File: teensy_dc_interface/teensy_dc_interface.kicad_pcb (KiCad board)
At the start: 2 copper layers, 80 x 128.5 mm, 165 parts, among them J1 Chan 1 Out, J10 3.5mm_Mono_Switched_SymSmall_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, J11 Conn_01x03, J12 Conn_01x03, J13 Conn_01x03, J2 Chan 2 Out, J3 Chan 3 Out, J4 Chan 4 Out, J5 Chan 5 Out, J6 Chan 6 Out, J7 Chan 7 Out, J8 Chan 8 Out, J9 3.5mm_Mono_Switched_SymSmall_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, U1 AK4458VN, U2 Teensy4.0, U3 AP65211A, U4 AP62200TWU-7, U5 NE5532, U6 NE5532, U7 NE5532, U8 NE5532, U9 AP65211A

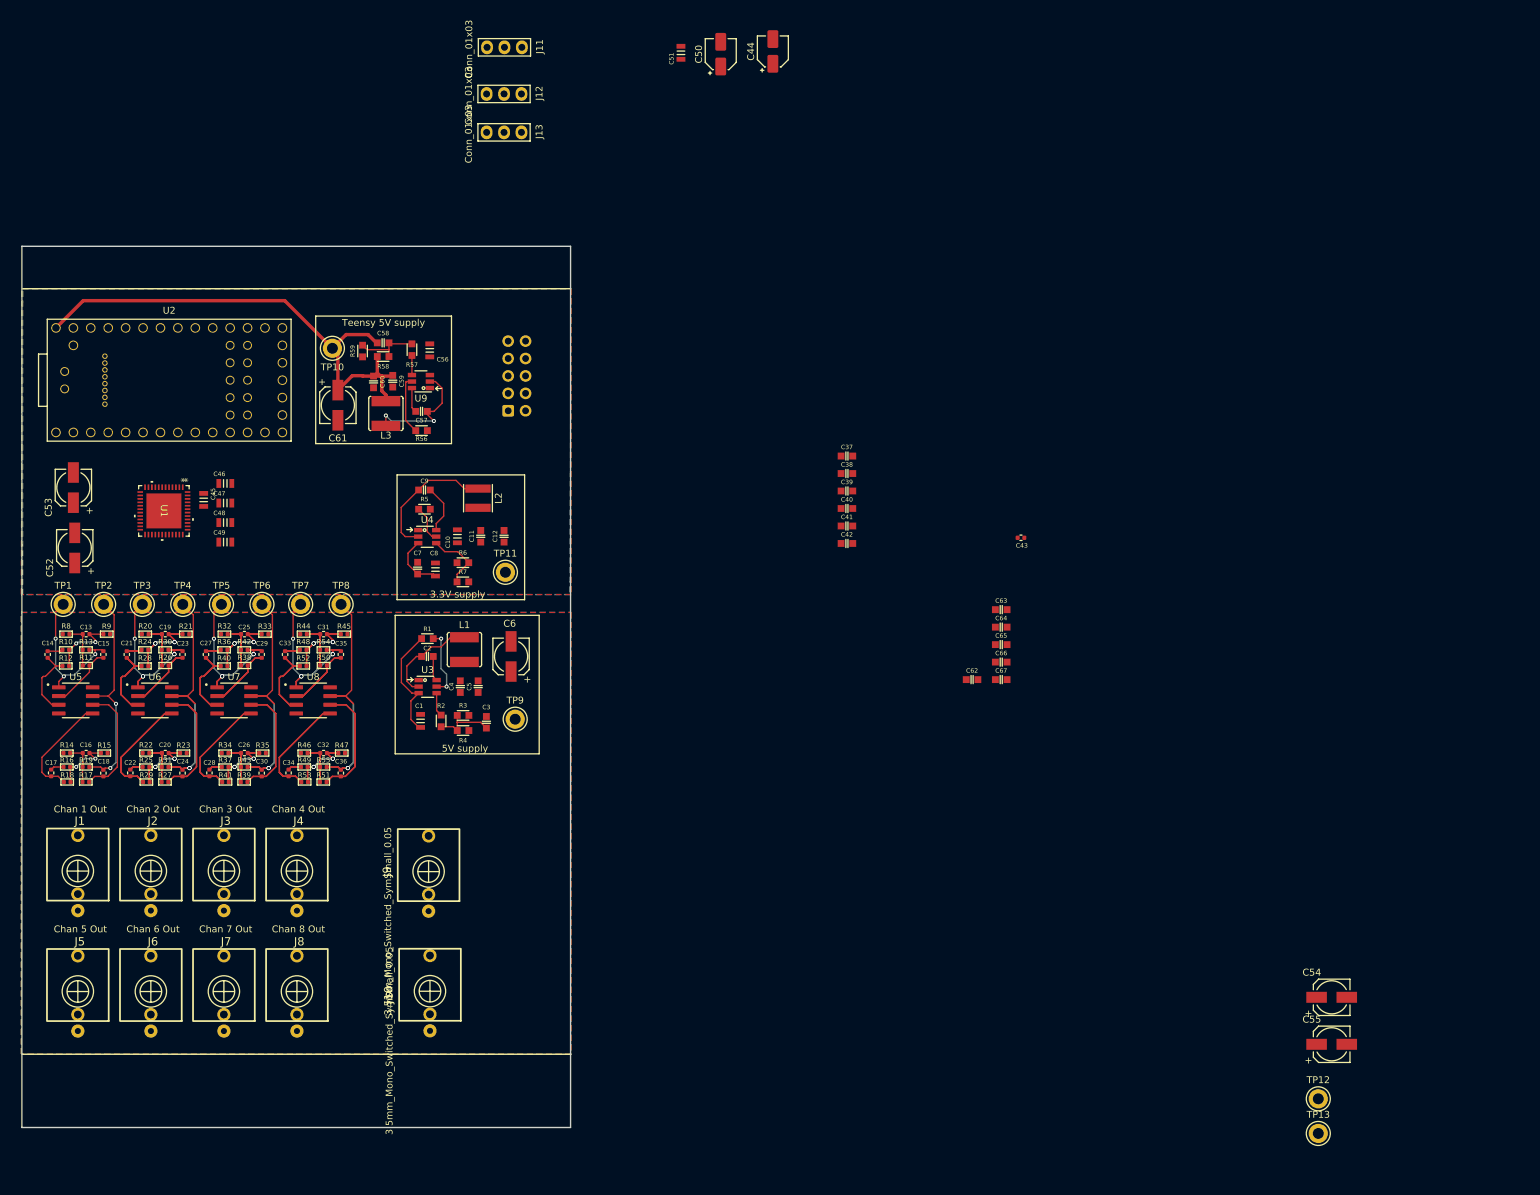
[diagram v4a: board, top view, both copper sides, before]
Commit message: Altered ground planes
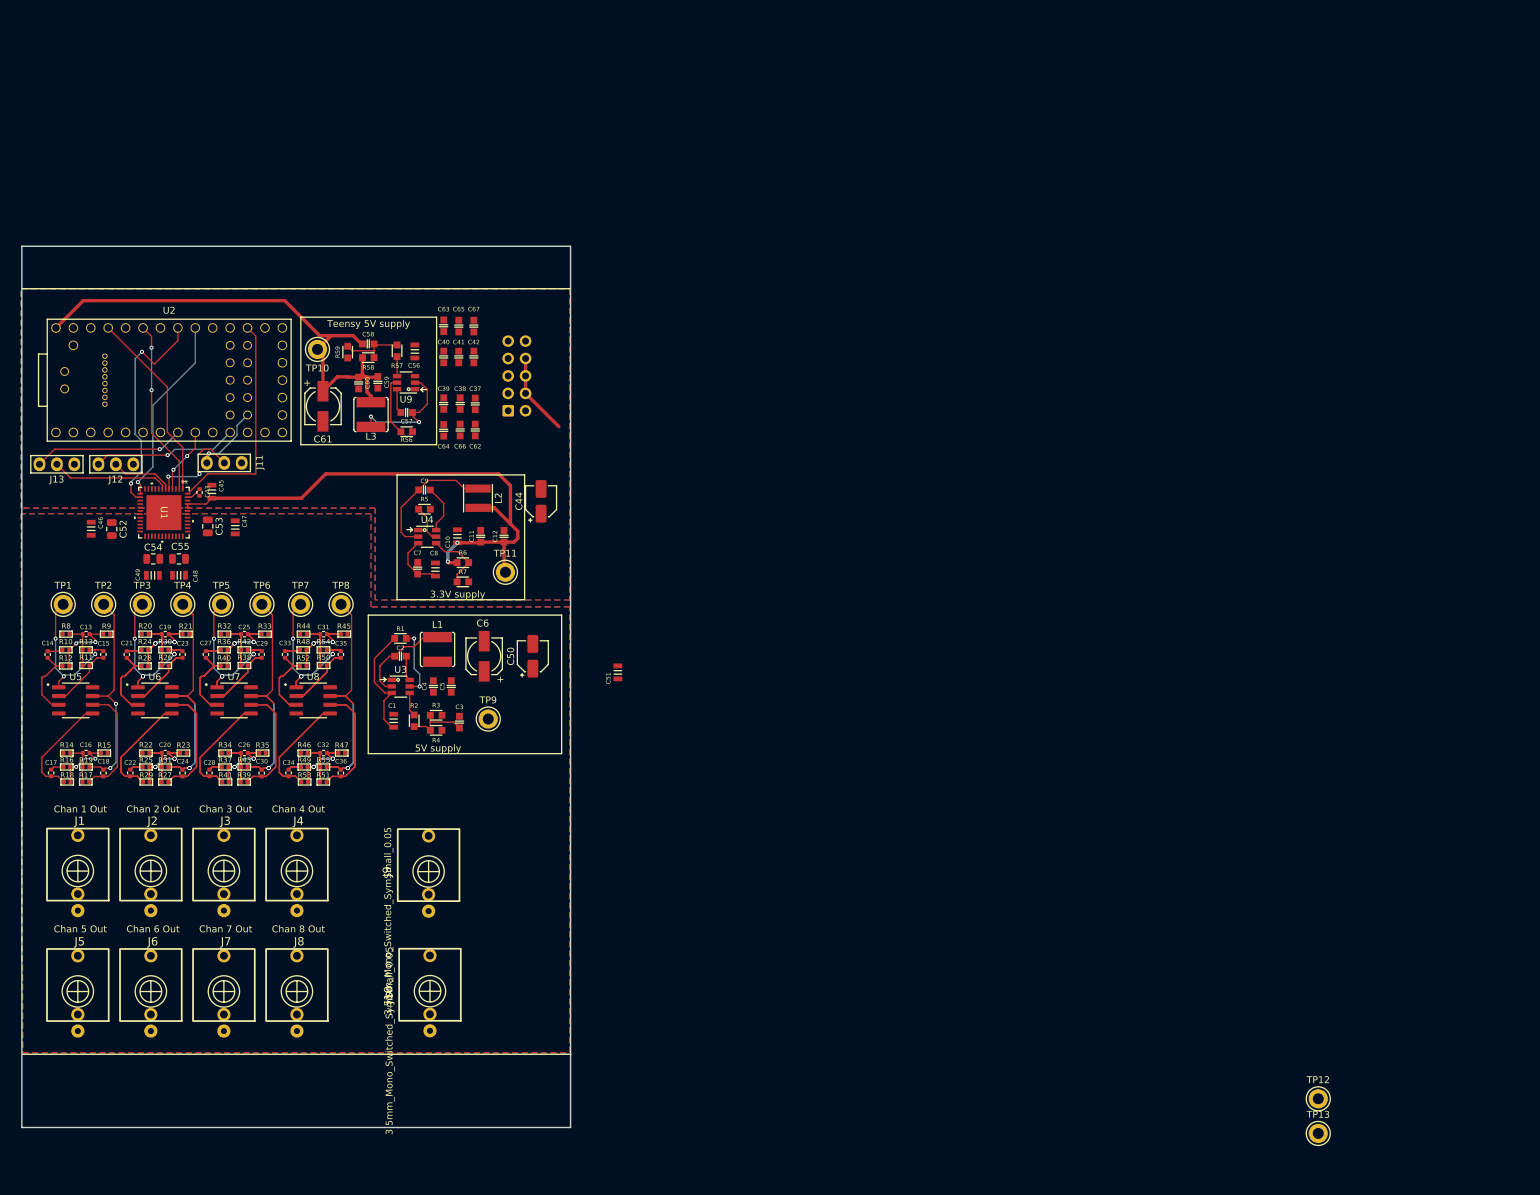
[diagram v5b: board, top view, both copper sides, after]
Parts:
- C52, C53, C54, C55: value 47uF_5x5.3_16V -> 47uF; footprint 4ms_Capacitor:CP_Elec_5x5.3 -> Capacitor_SMD:C_0805_2012Metric
- moved C54 183.3 mm to (50.2, 66.6)
- moved C55 182.4 mm to (54.0, 66.6), turned to 180 degrees
- moved C43 120.0 mm to (57.0, 56.9), turned to 90 degrees
- moved C67 92.6 mm to (97.0, 32.6), turned to -90 degrees
- moved C50 92.0 mm to (105.6, 80.8)
- moved C65 91.7 mm to (94.8, 32.6), turned to -90 degrees
- moved C63 91.2 mm to (92.6, 32.6), turned to -90 degrees
- moved C51 90.8 mm to (118.0, 83.2)
- moved C64 86.2 mm to (92.6, 47.9), turned to -90 degrees
- moved C66 85.9 mm to (95.0, 47.8), turned to -90 degrees
- moved J13 81.2 mm to (36.2, 52.8)
- moved C62 81.1 mm to (97.2, 47.8), turned to -90 degrees
- moved J12 78.2 mm to (44.8, 52.8)
- moved C44 73.8 mm to (106.8, 58.2)
- moved J11 73.1 mm to (60.6, 52.6)
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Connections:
- C52 pad 1: AVDD -> AVSS
- C52 pad 2: AVSS -> AVDD
- C53 pad 1: AVDD -> AVSS
- C53 pad 2: AVSS -> AVDD
- C54 pad 1: AVDD -> AVSS
- C54 pad 2: AVSS -> AVDD
- C55 pad 1: AVDD -> AVSS
- C55 pad 2: AVSS -> AVDD
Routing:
- net TVDD: track 0.00 -> 82.2 mm, vias 0 -> 2
- net PDN: track 0.00 -> 32.9 mm
- net SCL/CCLK/TDM1: track 0.00 -> 32.8 mm, vias 0 -> 2
- net MCLK: track 0.00 -> 28.0 mm
- net SDA/CDTI/TDM0: track 0.00 -> 27.8 mm, vias 0 -> 1
- net BICK/DCLK: track 0.00 -> 25.7 mm, vias 0 -> 2
- net 6_OUT1D: track 0.00 -> 22.1 mm, vias 0 -> 1
- net 9_OUT1C: track 0.00 -> 21.1 mm, vias 0 -> 1
- net SDTI4/DSDL3/TDMO2: track 0.00 -> 17.2 mm
- net SDTI2/DSDL2: track 0.00 -> 14.4 mm, vias 0 -> 2
- net AVSS: track 29.4 -> 41.3 mm
- net 32_OUT1B: track 0.00 -> 10.3 mm, vias 0 -> 1
- net SDTI1/DSDR1: track 0.00 -> 9.61 mm, vias 0 -> 2
- net SDTI3/DSDR2/TDMO1: track 0.00 -> 9.11 mm
- net VDD18: track 0.00 -> 2.23 mm
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
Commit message: connect rest of signal, add joining vias
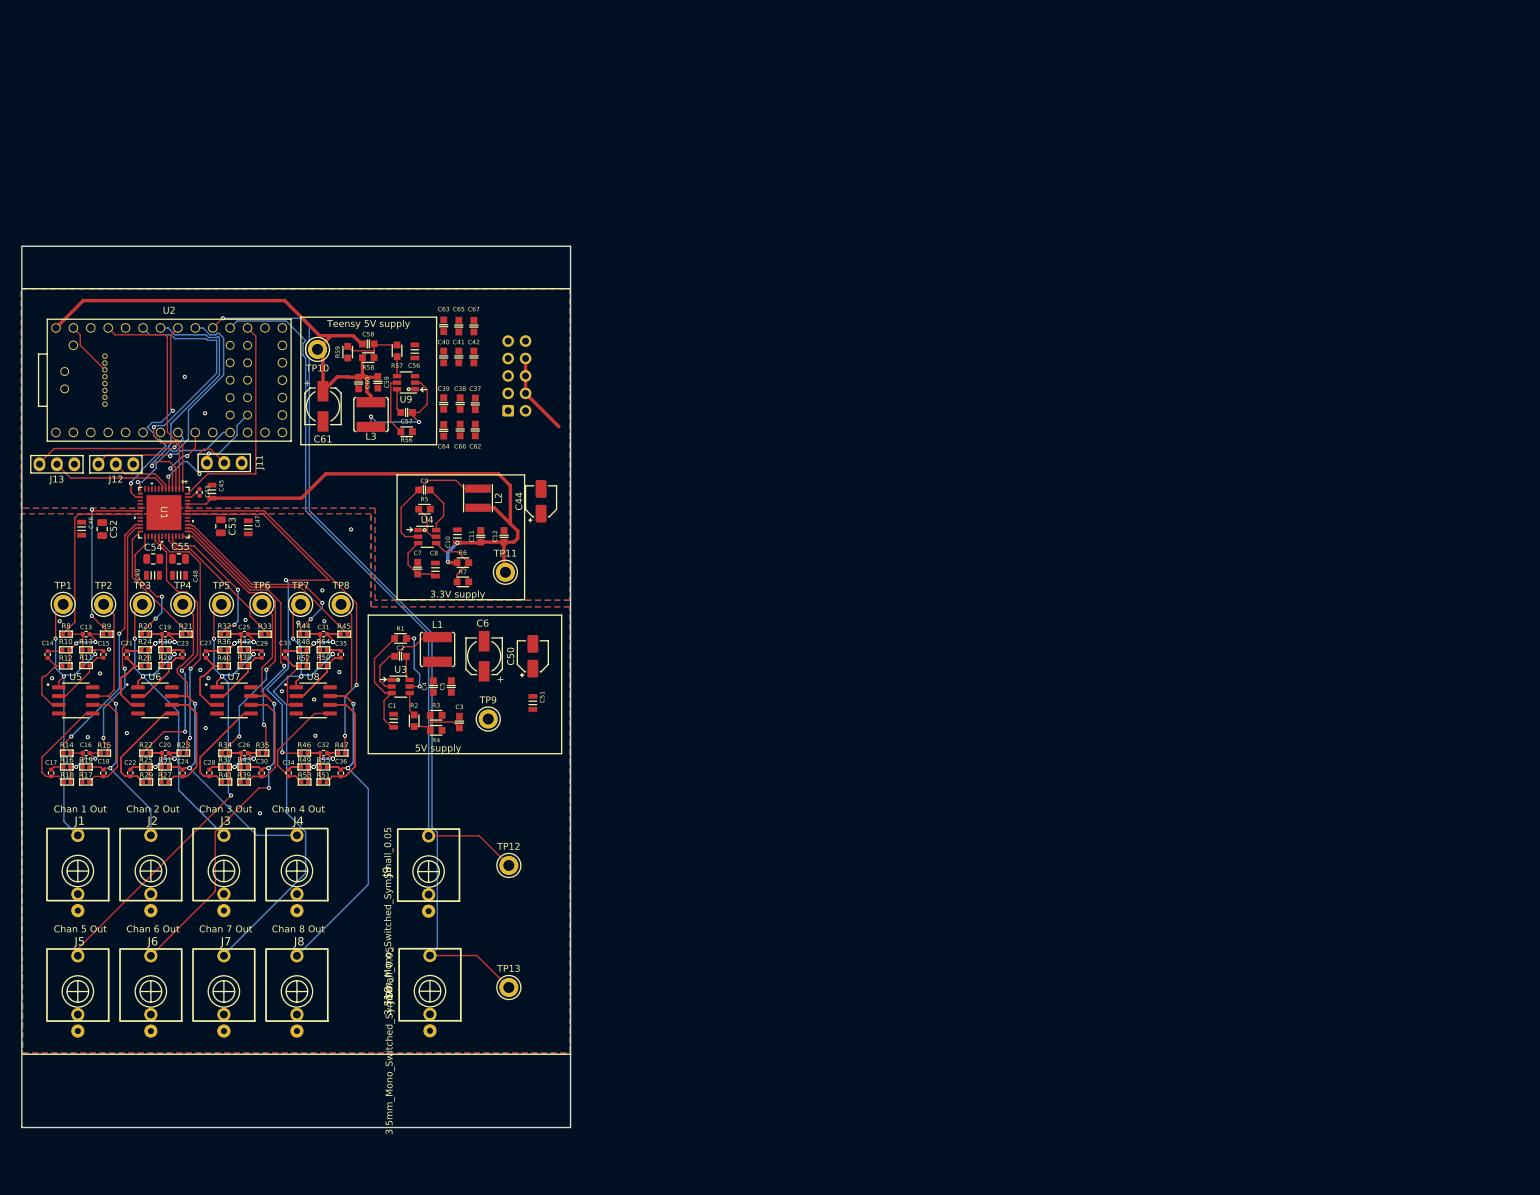
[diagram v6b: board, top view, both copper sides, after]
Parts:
- moved TP12 122.8 mm to (102.1, 111.3)
- moved TP13 119.9 mm to (102.1, 129.1)
- moved C51 13.2 mm to (105.6, 87.6), turned to -90 degrees
- moved C53 1.90 mm to (60.1, 61.9)
- moved C47 1.90 mm to (64.1, 62.0)
- moved C46 1.40 mm to (39.8, 62.2)
- moved C52 1.40 mm to (42.8, 62.2)
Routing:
- net ADC3: track 0.00 -> 129.1 mm, vias 0 -> 1
- net ADC2: track 0.00 -> 106.0 mm
- net /DAC/AOUTR4N: track 0.00 -> 61.2 mm, vias 0 -> 2
- net /DAC/AOUTR4P: track 0.00 -> 52.8 mm, vias 0 -> 2
- net /Outs/Out Pair 3/OP1_OUT: track 32.7 -> 83.2 mm, vias 5 -> 6
- net /Outs/Out Pair 4/OP1_OUT: track 32.7 -> 83.1 mm
- net /DAC/AOUTR3N: track 0.00 -> 42.9 mm, vias 0 -> 2
- net /DAC/AOUTR3P: track 0.00 -> 41.4 mm, vias 0 -> 2
- net /DAC/AOUTR2N: track 0.00 -> 40.4 mm, vias 0 -> 2
- net LRCK/DSDL1: track 0.00 -> 39.3 mm, vias 0 -> 1
- net /DAC/AOUTR1N: track 0.00 -> 38.4 mm, vias 0 -> 2
- net /DAC/AOUTR2P: track 0.00 -> 36.6 mm, vias 0 -> 2
- net /DAC/AOUTR1P: track 0.00 -> 35.9 mm, vias 0 -> 2
- net /Outs/Out Pair 3/OP2_OUT: track 48.2 -> 84.1 mm, vias 2 -> 4
- net /Outs/Out Pair 4/OP2_OUT: track 48.2 -> 81.1 mm, vias 2 -> 3
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
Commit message: Finished core electrical layout
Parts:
- moved C54 0.25 mm to (50.0, 66.6)
- moved C49 0.20 mm to (50.0, 69.0)
- moved C8 0.15 mm to (91.4, 68.0)
- moved C48 0.15 mm to (54.1, 69.0)
- moved C55 0.15 mm to (54.1, 66.6), turned to 0 degrees
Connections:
- C2 pad 1: /Power/SW -> Net-(U3-SW)
- C2 pad 2: /Power/BST -> Net-(U3-BST)
- C3 pad 1: /Power/FB -> Net-(C3-Pad1)
- C57 pad 1: /Power/SW -> Net-(U9-SW)
- C57 pad 2: /Power/BST -> Net-(U9-BST)
- C58 pad 1: /Power/FB -> Net-(C58-Pad1)
- L1 pad 1: /Power/SW -> Net-(U3-SW)
- L3 pad 1: /Power/SW -> Net-(U9-SW)
- R1 pad 1: /Power/EN -> Net-(U3-EN)
- R2 pad 2: /Power/FB -> Net-(C3-Pad1)
- R3 pad 1: /Power/FB -> Net-(C3-Pad1)
- R4 pad 2: /Power/FB -> Net-(C3-Pad1)
- R56 pad 1: /Power/EN -> Net-(U9-EN)
- R57 pad 2: /Power/FB -> Net-(C58-Pad1)
- R58 pad 1: /Power/FB -> Net-(C58-Pad1)
- R59 pad 2: /Power/FB -> Net-(C58-Pad1)
- R6 pad 2: /Power/FB -> Net-(U4-FB)
- R7 pad 1: /Power/FB -> Net-(U4-FB)
- U3 pad 2: /Power/SW -> Net-(U3-SW)
- U3 pad 5: /Power/EN -> Net-(U3-EN)
- U3 pad 6: /Power/BST -> Net-(U3-BST)
- U4 pad 4: /Power/FB -> Net-(U4-FB)
- U9 pad 2: /Power/SW -> Net-(U9-SW)
- U9 pad 5: /Power/EN -> Net-(U9-EN)
- U9 pad 6: /Power/BST -> Net-(U9-BST)
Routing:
- net +12V: track 25.4 -> 341.4 mm, vias 0 -> 12
- net AVSS: track 41.3 -> 223.3 mm, vias 20 -> 75
- net -12VA: track 0.00 -> 176.5 mm, vias 0 -> 6
- net AVDD: track 0.00 -> 155.1 mm, vias 0 -> 7
- net /Power/SW: track 51.7 -> 19.7 mm, vias 2 -> 0
- net /Power/FB: track 28.3 -> 0.00 mm
- net DVSS: track 8.02 -> 35.8 mm, vias 2 -> 15
- net TVDD: track 82.2 -> 104.9 mm, vias 2 -> 4
- net /Power/EN: track 18.5 -> 0.00 mm, vias 2 -> 0
- net Net-(U9-SW): track 0.00 -> 17.6 mm, vias 0 -> 2
- net Net-(U3-SW): track 0.00 -> 14.4 mm
- net /Outs/Out Pair 2/OP2_NEG: track 33.9 -> 22.1 mm
- net Net-(U3-EN): track 0.00 -> 9.94 mm, vias 0 -> 2
- net /Outs/Out Pair 3/OP2_OUT: track 84.1 -> 74.3 mm, vias 4 -> 3
- net Net-(C58-Pad1): track 0.00 -> 9.53 mm
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
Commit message: checks, added silkscreens
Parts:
- moved J11 4.56 mm to (65.2, 52.8)
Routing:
- net PDN: track 36.7 -> 46.7 mm
- net 32_OUT1B: track 10.3 -> 7.75 mm, vias 1 -> 0
- net SDTI2/DSDL2: track 15.9 -> 17.2 mm, vias 2 -> 1
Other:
- board size 80 x 128.5 mm -> 80.9 x 128.5 mm
- board text added: "2"
- board text added: "3"
- board text added: "4"
- board text added: "CH1"
- board text added: "CH2"
- board text added: "CH3"
- board text added: "CH4"
- board text added: "CH5"
- board text added: "CH6"
- board text added: "CH7"
- board text added: "CH8"
- board text added: "Chan 1 In"
- board text added: "Chan 2 In"
- board text added: "I2S"
- board text added: "TDM"
